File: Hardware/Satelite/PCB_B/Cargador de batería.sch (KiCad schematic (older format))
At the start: 7 parts, among them U8 BQ24091DGQT

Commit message: Arreglos en PCB_A y PCB_B:
- El CI cargador de batería ya no alimenta al sistema, al conectar un cargador el mismo alimenta a la batería y al sistema de manera simultánea
- Ya no es necesario encender el CanSat para cargar la batería
- El interruptor del PCB_A ahora apaga todo el sistema independientemente si se está cargando o no la batería
- Agregado LED indicador de carga de batería
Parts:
- removed R15: 2k, Resistor_SMD:R_0603_1608Metric_Pad1.05x0.95mm_HandSolder, symbol Device:R
- removed R16: 100k, Resistor_SMD:R_0603_1608Metric_Pad1.05x0.95mm_HandSolder, symbol Device:R
- removed U8: BQ24091DGQT, SamacSys_Parts:SOP50P490X110-11N, symbol SamacSys_Parts:BQ24091DGQT
- added TH1: Thermistor_NTC, Resistor_SMD:R_0603_1608Metric_Pad1.05x0.95mm_HandSolder, symbol Device:Thermistor_NTC
- added U10: BQ21040DBVR, SOT95P280X145-6N, symbol SamacSys_Parts:BQ21040DBVR
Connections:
- net labels removed: CHG_DISABLE, ISET
- wire segments 26 -> 18
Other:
- note added: "El termistor debe estar en contacto\ndirecto con la batería"
- note removed: "Corriente de pre-carga 20% de carga"
- note removed: "Corriente de terminación 10% de carga"
- moved on the sheet: C25, C26, R14, R22

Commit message: PCB_B V2 terminado
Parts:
- removed TH1: Thermistor_NTC, Resistor_SMD:R_0603_1608Metric_Pad1.05x0.95mm_HandSolder, symbol Device:Thermistor_NTC
- added R19: 100k, Resistor_SMD:R_0603_1608Metric_Pad1.05x0.95mm_HandSolder, symbol Device:R
- U10: footprint SOT95P280X145-6N -> SamacSys_Parts:SOT95P280X145-6N
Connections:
- net GND: now also R19.1
- net at U10.1 (TS): now also R19.2
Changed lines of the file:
@@
 F 0 "U10" H 6900 3815 50  0000 C CNN
 F 1 "BQ21040DBVR" H 6900 3724 50  0000 C CNN
-F 2 "SOT95P280X145-6N" H 7300 3650 50  0001 L CNN
+F 2 "SamacSys_Parts:SOT95P280X145-6N" H 7300 3650 50  0001 L CNN
 F 3 "http://www.ti.com/lit/gpn/bq21040" H 7300 3550 50  0001 L CNN
 F 4 "0.8A Single Input Single-Cell Li-Ion and Li-Pol Battery Charger" H 7300 3450 50  0001 L CNN "Description"
@@
 	7050 3750 6350 3750
 $Comp
-L Device:Thermistor_NTC TH1
-U 1 1 5CC9077E
-P 6700 4150
-F 0 "TH1" H 6547 4104 50  0000 R CNN
-F 1 "Thermistor_NTC" H 6547 4195 50  0000 R CNN
-F 2 "Resistor_SMD:R_0603_1608Metric_Pad1.05x0.95mm_HandSolder" H 6700 4200 50  0001 C CNN
-F 3 "~" H 6700 4200 50  0001 C CNN
-F 4 "P12013CT-ND" H 6700 4150 50  0001 C CNN "Manufacturer Part Number"
-	1    6700 4150
-	1    0    0    1
-$EndComp
-$Comp
 L power:GND #PWR?
 U 1 1 5CC95641
@@
 Text Notes 6200 4750 0    50   ~ 0
 El termistor debe estar en contacto\ndirecto con la batería
+$Comp
+L Device:R R?
+U 1 1 5CD36697
+P 6700 4150
+AR Path="/5BA17F9C/5CD36697" Ref="R?"  Part="1"
+AR Path="/5BA1A7F9/5CD36697" Ref="R?"  Part="1"
+AR Path="/5BA1A77A/5CD36697" Ref="R?"  Part="1"
+AR Path="/5BC300BF/5CD36697" Ref="R19"  Part="1"
+F 0 "R19" V 6800 4150 50  0000 L CNN
+F 1 "100k" V 6600 4050 50  0000 L CNN
+F 2 "Resistor_SMD:R_0603_1608Metric_Pad1.05x0.95mm_HandSolder" V 6630 4150 50  0001 C CNN
+F 3 "~" H 6700 4150 50  0001 C CNN
+F 4 "RC0603JR-07100KL" V 6700 4150 50  0001 C CNN "Manufacturer Part Number"
+	1    6700 4150
+	-1   0    0    1
+$EndComp
 $EndSCHEMATC

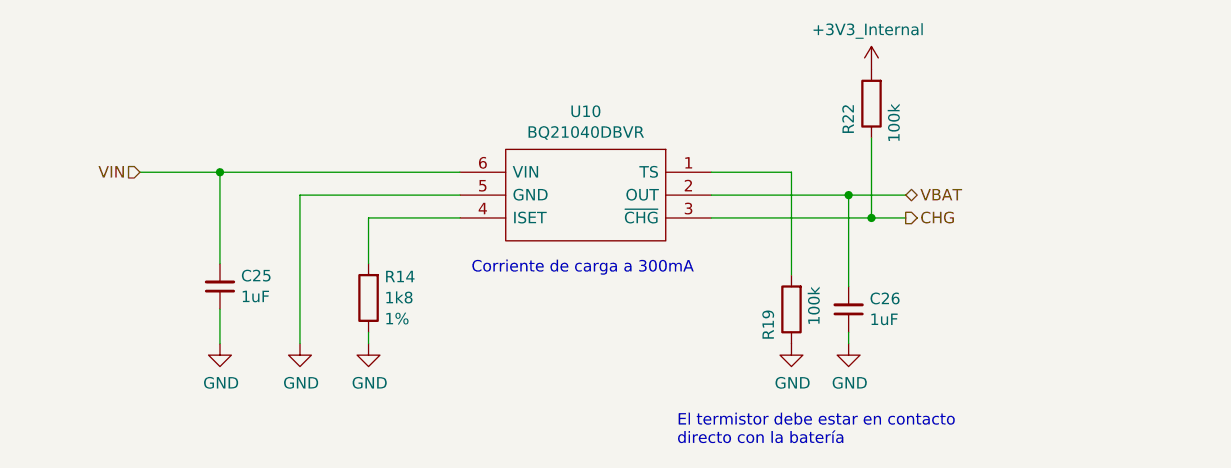
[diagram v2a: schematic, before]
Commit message: Eliminado termistor de PCB_B
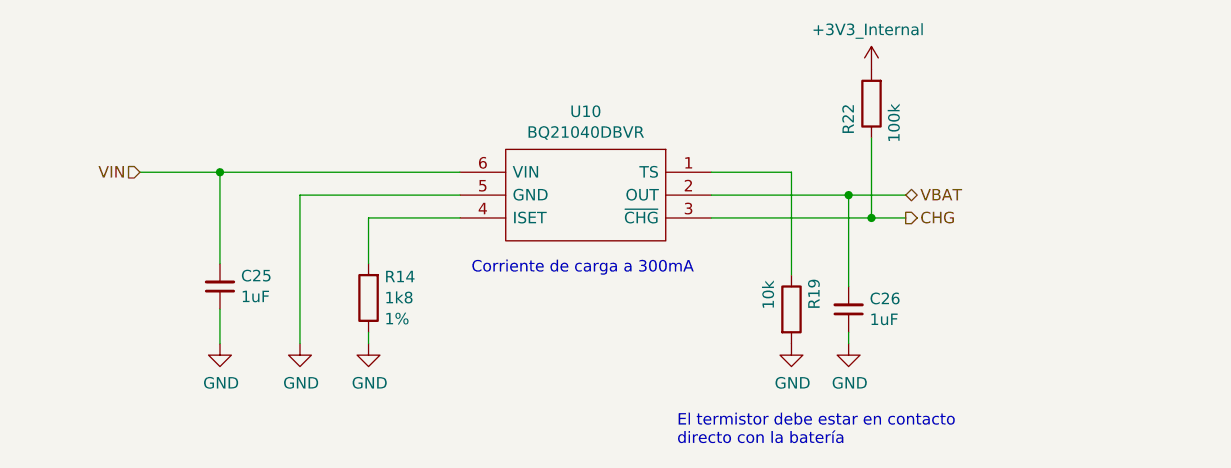
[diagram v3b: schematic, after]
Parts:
- R19: value 100k -> 10k; footprint Resistor_SMD:R_0603_1608Metric_Pad1.05x0.95mm_HandSolder -> Capacitor_SMD:C_0603_1608Metric_Pad1.05x0.95mm_HandSolder; Manufacturer Part Number RC0603JR-07100KL -> RC0603JR-0710KL
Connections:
- net GND: now also R19.2; no longer R19.1
- net at U10.1 (TS): now also R19.1; no longer R19.2
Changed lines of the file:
@@
 $Comp
 L Device:R R?
-U 1 1 5CD36697
+U 1 1 5CD971D1
 P 6700 4150
-AR Path="/5BA17F9C/5CD36697" Ref="R?"  Part="1"
-AR Path="/5BA1A7F9/5CD36697" Ref="R?"  Part="1"
-AR Path="/5BA1A77A/5CD36697" Ref="R?"  Part="1"
-AR Path="/5BC300BF/5CD36697" Ref="R19"  Part="1"
+AR Path="/5BA17F9C/5CD971D1" Ref="R?"  Part="1"
+AR Path="/5BA1A7F9/5CD971D1" Ref="R?"  Part="1"
+AR Path="/5BA1A77A/5CD971D1" Ref="R?"  Part="1"
+AR Path="/5CD971D1" Ref="R?"  Part="1"
+AR Path="/5BB1631B/5CD971D1" Ref="R?"  Part="1"
+AR Path="/5BC28DAC/5CD971D1" Ref="R?"  Part="1"
+AR Path="/5BC300BF/5CD971D1" Ref="R19"  Part="1"
 F 0 "R19" V 6800 4150 50  0000 L CNN
-F 1 "100k" V 6600 4050 50  0000 L CNN
-F 2 "Resistor_SMD:R_0603_1608Metric_Pad1.05x0.95mm_HandSolder" V 6630 4150 50  0001 C CNN
+F 1 "10k" V 6600 4150 50  0000 L CNN
+F 2 "Capacitor_SMD:C_0603_1608Metric_Pad1.05x0.95mm_HandSolder" V 6630 4150 50  0001 C CNN
 F 3 "~" H 6700 4150 50  0001 C CNN
-F 4 "RC0603JR-07100KL" V 6700 4150 50  0001 C CNN "Manufacturer Part Number"
+F 4 "RC0603JR-0710KL" V 6700 4150 50  0001 C CNN "Manufacturer Part Number"
 	1    6700 4150
-	-1   0    0    1
+	1    0    0    -1
 $EndComp
 $EndSCHEMATC

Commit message: PCB_B BOM
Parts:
- U10: Manufacturer Part Number (none) -> BQ21040DBVR; Manufacturer_Part_Number BQ21040DBVR -> (none)
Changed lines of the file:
@@
 F 5 "1.45" H 7300 3350 50  0001 L CNN "Height"
 F 6 "Texas Instruments" H 7300 3250 50  0001 L CNN "Manufacturer_Name"
-F 7 "BQ21040DBVR" H 7300 3150 50  0001 L CNN "Manufacturer_Part_Number"
+F 7 "BQ21040DBVR" H 7300 3150 50  0001 L CNN "Manufacturer Part Number"
 F 8 "595-BQ21040DBVR" H 7300 3050 50  0001 L CNN "Mouser Part Number"
 F 9 "https://www.mouser.com/Search/Refine.aspx?Keyword=595-BQ21040DBVR" H 7300 2950 50  0001 L CNN "Mouser Price/Stock"
